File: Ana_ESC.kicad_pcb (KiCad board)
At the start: 2 copper layers, 57 parts, among them Q1 STB75NF75T4, Q2 STB75NF75T4, Q3 STB75NF75T4, Q4 STB75NF75T4, Q5 STB75NF75T4, Q6 STB75NF75T4, U1 DRV8323RSRGZR, U2 STM32G431CBU6

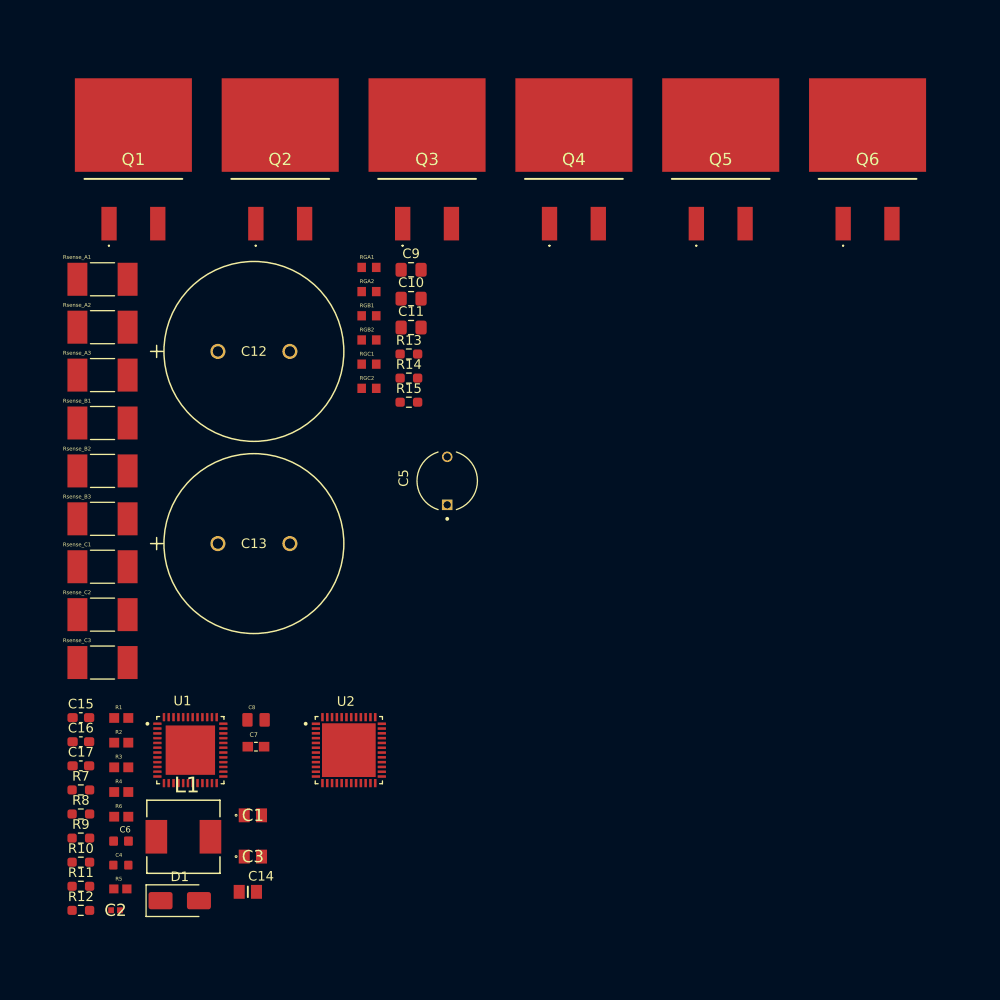
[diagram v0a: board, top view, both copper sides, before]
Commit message: thermal calculations done and Shunt Resistors changed. Not 3, just 2 resistors can dissipate the power.
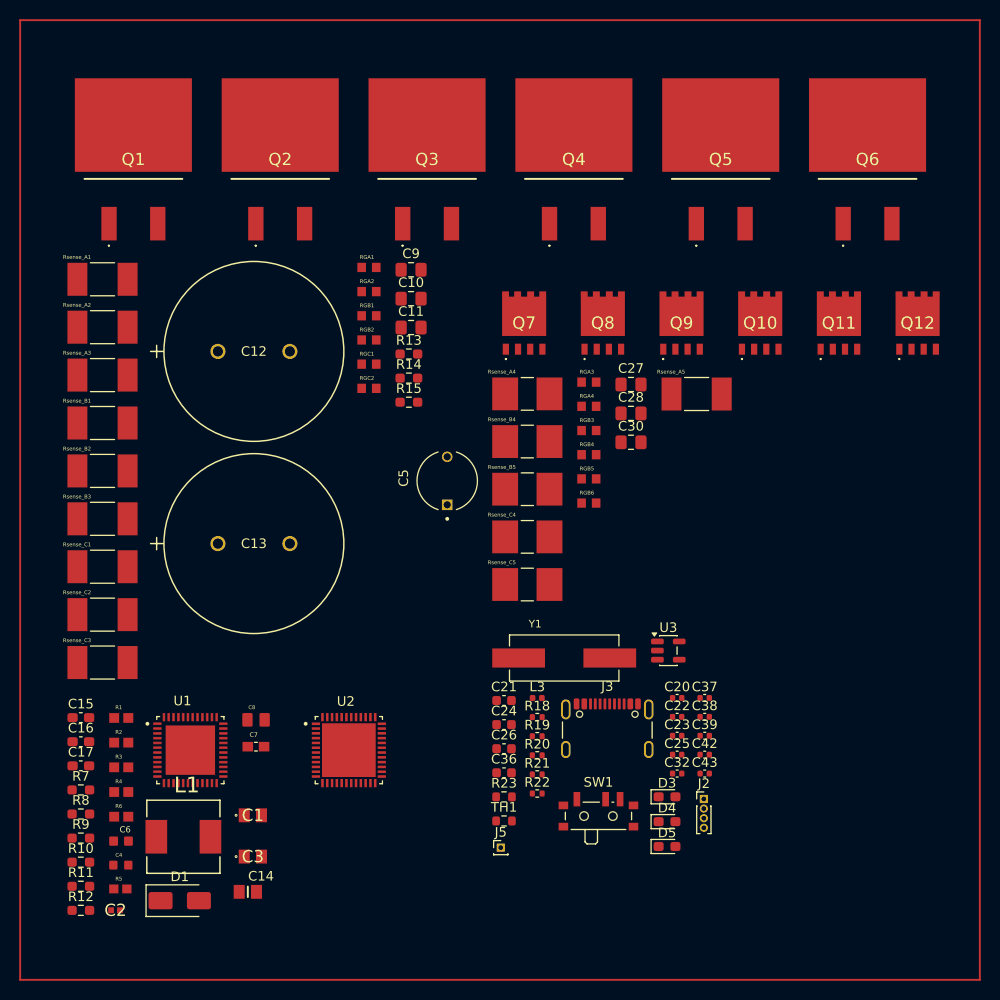
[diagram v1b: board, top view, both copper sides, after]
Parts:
- added C20: 100nF, Capacitor_SMD:C_0402_1005Metric, F.Cu at (132.5, 133.1)
- added C21: 1uF, Capacitor_SMD:C_0603_1608Metric, F.Cu at (114.4, 133.4)
- added C22: 1u, Capacitor_SMD:C_0402_1005Metric, F.Cu at (132.5, 135.1)
- added C23: 1u, Capacitor_SMD:C_0402_1005Metric, F.Cu at (132.5, 137.1)
- added C24: 2.2uF, Capacitor_SMD:C_0603_1608Metric, F.Cu at (114.4, 135.9)
- added C25: 100n, Capacitor_SMD:C_0402_1005Metric, F.Cu at (132.5, 139.0)
- added C26: 1uF, Capacitor_SMD:C_0603_1608Metric, F.Cu at (114.4, 138.4)
- added C27: 2.2uF, Capacitor_SMD:C_0805_2012Metric_Pad1.18x1.45mm_HandSolder, F.Cu at (127.7, 100.5)
- added C28: 2.2uF, Capacitor_SMD:C_0805_2012Metric_Pad1.18x1.45mm_HandSolder, F.Cu at (127.7, 103.5)
- added C30: 2.2uF, Capacitor_SMD:C_0805_2012Metric_Pad1.18x1.45mm_HandSolder, F.Cu at (127.7, 106.5)
- added C32: 100n, Capacitor_SMD:C_0402_1005Metric, F.Cu at (132.5, 141.0)
- added C36: 4u7, Capacitor_SMD:C_0603_1608Metric, F.Cu at (114.4, 140.9)
- added C37: 100n, Capacitor_SMD:C_0402_1005Metric, F.Cu at (135.3, 133.1)
- added C38: 100n, Capacitor_SMD:C_0402_1005Metric, F.Cu at (135.3, 135.1)
- added C39: 100n, Capacitor_SMD:C_0402_1005Metric, F.Cu at (135.3, 137.1)
- added C42: 1u, Capacitor_SMD:C_0402_1005Metric, F.Cu at (135.3, 139.0)
- added C43: 10n, Capacitor_SMD:C_0402_1005Metric, F.Cu at (135.3, 141.0)
- added D3: LEDA, LED_SMD:LED_0603_1608Metric_Pad1.05x0.95mm_HandSolder, F.Cu at (131.4, 143.4)
- added D4: LEDB, LED_SMD:LED_0603_1608Metric_Pad1.05x0.95mm_HandSolder, F.Cu at (131.4, 146.0)
- added D5: LEDC, LED_SMD:LED_0603_1608Metric_Pad1.05x0.95mm_HandSolder, F.Cu at (131.4, 148.6)
- added J2: Conn_01x04_Pin, Connector_PinHeader_1.00mm:PinHeader_1x04_P1.00mm_Vertical, F.Cu at (135.2, 143.7)
- added J3: USB_C_Receptacle_USB2.0_16P, Connector_USB:USB_C_Receptacle_GCT_USB4105-xx-A_16P_TopMnt_Horizontal, F.Cu at (125.2, 137.4)
- added J5: Conn_01x01_Pin, Connector_PinHeader_1.00mm:PinHeader_1x01_P1.00mm_Vertical, F.Cu at (114.1, 148.7)
- added L3: 100MHz / 1kR, Inductor_SMD:L_0402_1005Metric, F.Cu at (117.9, 133.1)
- added Q10: STL90N6F7, STL90N6F7:STL90N6F7, F.Cu at (141.1, 94.1)
- added Q11: STL90N6F7, STL90N6F7:STL90N6F7, F.Cu at (149.3, 94.1)
- added Q12: STL90N6F7, STL90N6F7:STL90N6F7, F.Cu at (157.5, 94.1)
- added Q7: STL90N6F7, STL90N6F7:STL90N6F7, F.Cu at (116.5, 94.1)
- added Q8: STL90N6F7, STL90N6F7:STL90N6F7, F.Cu at (124.7, 94.1)
- added Q9: STL90N6F7, STL90N6F7:STL90N6F7, F.Cu at (132.9, 94.1)
- added R18: 10k, Resistor_SMD:R_0402_1005Metric, F.Cu at (117.9, 135.1)
- added R19: 120R, Resistor_SMD:R_0402_1005Metric, F.Cu at (117.9, 137.1)
- added R20: 10k, Resistor_SMD:R_0402_1005Metric, F.Cu at (117.9, 139.1)
- added R21: 10k, Resistor_SMD:R_0402_1005Metric, F.Cu at (117.9, 141.1)
- added R22: 10k, Resistor_SMD:R_0402_1005Metric, F.Cu at (117.9, 143.1)
- added R23: R_Small, Resistor_SMD:R_0603_1608Metric, F.Cu at (114.4, 143.4)
- added RGA3: 0ohm, RMCF0603ZT0R00:RESC1508X55N, F.Cu at (123.3, 100.2)
- added RGA4: 0ohm, RMCF0603ZT0R00:RESC1508X55N, F.Cu at (123.3, 102.7)
- added RGB3: 0ohm, RMCF0603ZT0R00:RESC1508X55N, F.Cu at (123.3, 105.3)
- added RGB4: 0ohm, RMCF0603ZT0R00:RESC1508X55N, F.Cu at (123.3, 107.8)
- added RGB5: 0ohm, RMCF0603ZT0R00:RESC1508X55N, F.Cu at (123.3, 110.3)
- added RGB6: 0ohm, RMCF0603ZT0R00:RESC1508X55N, F.Cu at (123.3, 112.8)
- added Rsense_A4: 2mohm, CRF2512-FZ-R002ELF:RESC6432X80N, F.Cu at (116.8, 101.4)
- added Rsense_A5: 2mohm, CSNL2512FT3L00:RESC6331X75N, F.Cu at (134.5, 101.5)
- added Rsense_B4: 2mohm, CRF2512-FZ-R002ELF:RESC6432X80N, F.Cu at (116.8, 106.4)
- added Rsense_B5: 2mohm, CRF2512-FZ-R002ELF:RESC6432X80N, F.Cu at (116.8, 111.4)
- added Rsense_C4: 2mohm, CRF2512-FZ-R002ELF:RESC6432X80N, F.Cu at (116.8, 116.3)
- added Rsense_C5: 2mohm, CRF2512-FZ-R002ELF:RESC6432X80N, F.Cu at (116.8, 121.3)
- added SW1: SW_SPDT, Button_Switch_SMD:SW_SPDT_PCM12, F.Cu at (124.3, 145.1)
- added TH1: ERT-J1VG103FA, Resistor_SMD:R_0603_1608Metric, F.Cu at (114.4, 145.9)
- added U3: ME6211C33M5, Package_TO_SOT_SMD:SOT-23-5, F.Cu at (131.5, 128.2)
- added Y1: ECS-80-20-5PX-TR, ECS-80-20-5PX-TR:XTAL_ECS-80-20-5PX-TR, F.Cu at (120.7, 129.0)
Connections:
- U2 pad 1: unconnected-(U2-VBAT-Pad1) -> +3.3V
- U2 pad 10: unconnected-(U2-PA2-Pad10) -> /Gate_Driver/SOA
- U2 pad 11: unconnected-(U2-PA3-Pad11) -> /Gate_Driver/SENS1
- U2 pad 13: unconnected-(U2-PA5-Pad13) -> /Gate_Driver/SENS2
- U2 pad 14: unconnected-(U2-PA6-Pad14) -> /MCU/NTC_FET
- U2 pad 15: unconnected-(U2-PA7-Pad15) -> /MCU/NTC_MTR
- U2 pad 17: unconnected-(U2-PB0-Pad17) -> /Gate_Driver/INLB
- U2 pad 18: unconnected-(U2-PB1-Pad18) -> /Gate_Driver/INLC
- U2 pad 19: unconnected-(U2-PB2-Pad19) -> /MCU/VBus
- U2 pad 2: unconnected-(U2-PC13-Pad2) -> /Gate_Driver/INLA
- U2 pad 20: unconnected-(U2-VREF+-Pad20) -> +3.3VA
- U2 pad 21: unconnected-(U2-VDDA-Pad21) -> +3.3VA
- U2 pad 23: VDD -> +3.3V
- U2 pad 24: unconnected-(U2-PB11-Pad24) -> /Gate_Driver/SENS3
- U2 pad 25: unconnected-(U2-PB12-Pad25) -> Net-(D3-A)
- U2 pad 26: unconnected-(U2-PB13-Pad26) -> Net-(D4-A)
- U2 pad 27: unconnected-(U2-PB14-Pad27) -> Net-(D5-A)
- U2 pad 30: unconnected-(U2-PA8-Pad30) -> /Gate_Driver/INHA
- U2 pad 31: unconnected-(U2-PA9-Pad31) -> /Gate_Driver/INHB
- U2 pad 32: unconnected-(U2-PA10-Pad32) -> /Gate_Driver/INHC
- U2 pad 33: unconnected-(U2-PA11-Pad33) -> /MCU/USB_DN
- U2 pad 34: unconnected-(U2-PA12-Pad34) -> /MCU/USB_DP
- U2 pad 35: VDD -> +3.3V
- U2 pad 36: unconnected-(U2-PA13-Pad36) -> /MCU/SWDIO
- U2 pad 37: unconnected-(U2-PA14-Pad37) -> /MCU/SWCLK
- U2 pad 38: unconnected-(U2-PA15-Pad38) -> /MCU/I2C1_SCL
- U2 pad 39: unconnected-(U2-PC10-Pad39) -> /MCU/UART_N
- U2 pad 40: unconnected-(U2-PC11-Pad40) -> /MCU/UART_P
- U2 pad 45: unconnected-(U2-PB7-Pad45) -> /MCU/I2C1_SDA
- U2 pad 46: unconnected-(U2-PB8-BOOT0-Pad46) -> /MCU/BOOT0
- U2 pad 48: VDD -> +3.3V
- U2 pad 49: unconnected-(U2-VSS-Pad49) -> GND
- U2 pad 5: unconnected-(U2-PF0-OSC_IN-Pad5) -> Net-(U2-PF0-OSC_IN)
- U2 pad 6: unconnected-(U2-PF1-OSC_OUT-Pad6) -> Net-(U2-PF1-OSC_OUT)
- U2 pad 7: unconnected-(U2-PG10-~{RST}-Pad7) -> /MCU/RST
- U2 pad 8: unconnected-(U2-PA0-Pad8) -> /Gate_Driver/SOC
- U2 pad 9: unconnected-(U2-PA1-Pad9) -> /Gate_Driver/SOB
